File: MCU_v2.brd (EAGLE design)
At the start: 66 x 51.2 mm, 29 parts, among them IC1 ATMEGA2560-16AU

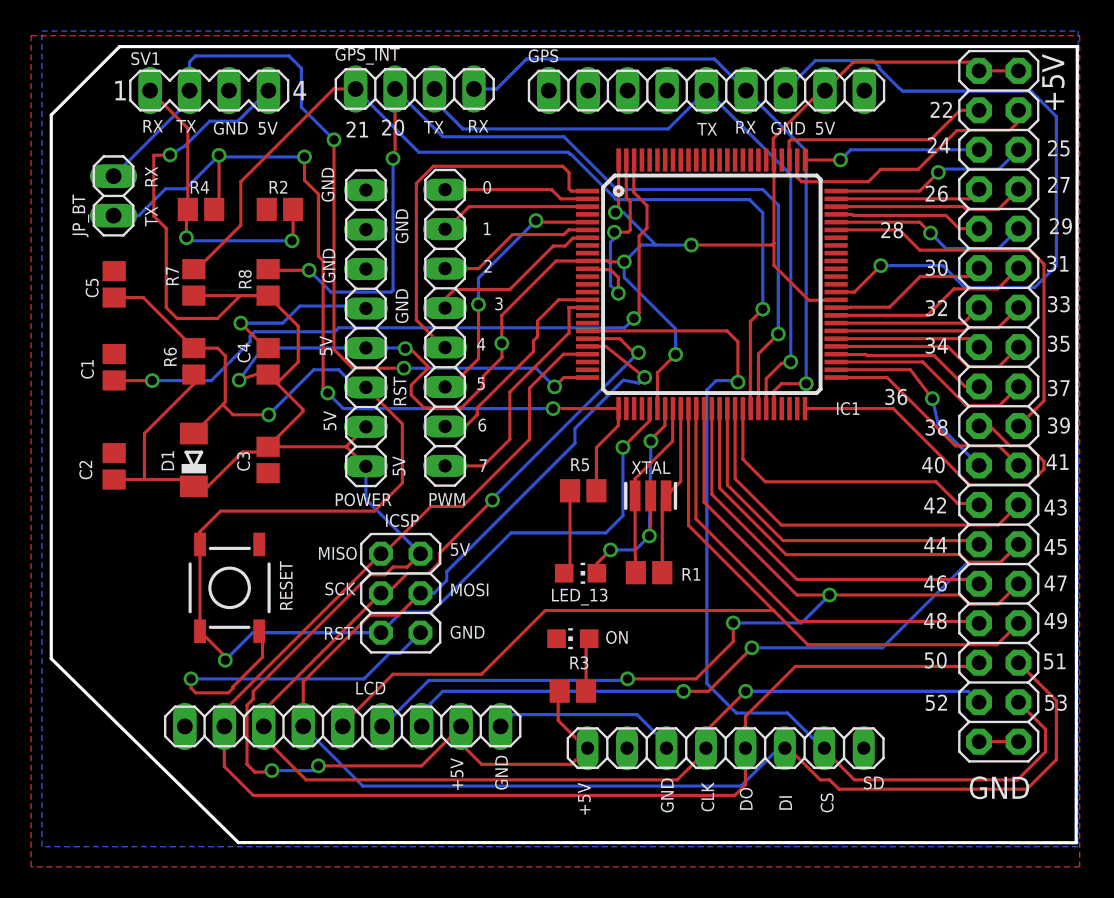
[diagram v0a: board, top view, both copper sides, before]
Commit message: Made the power traces thicker
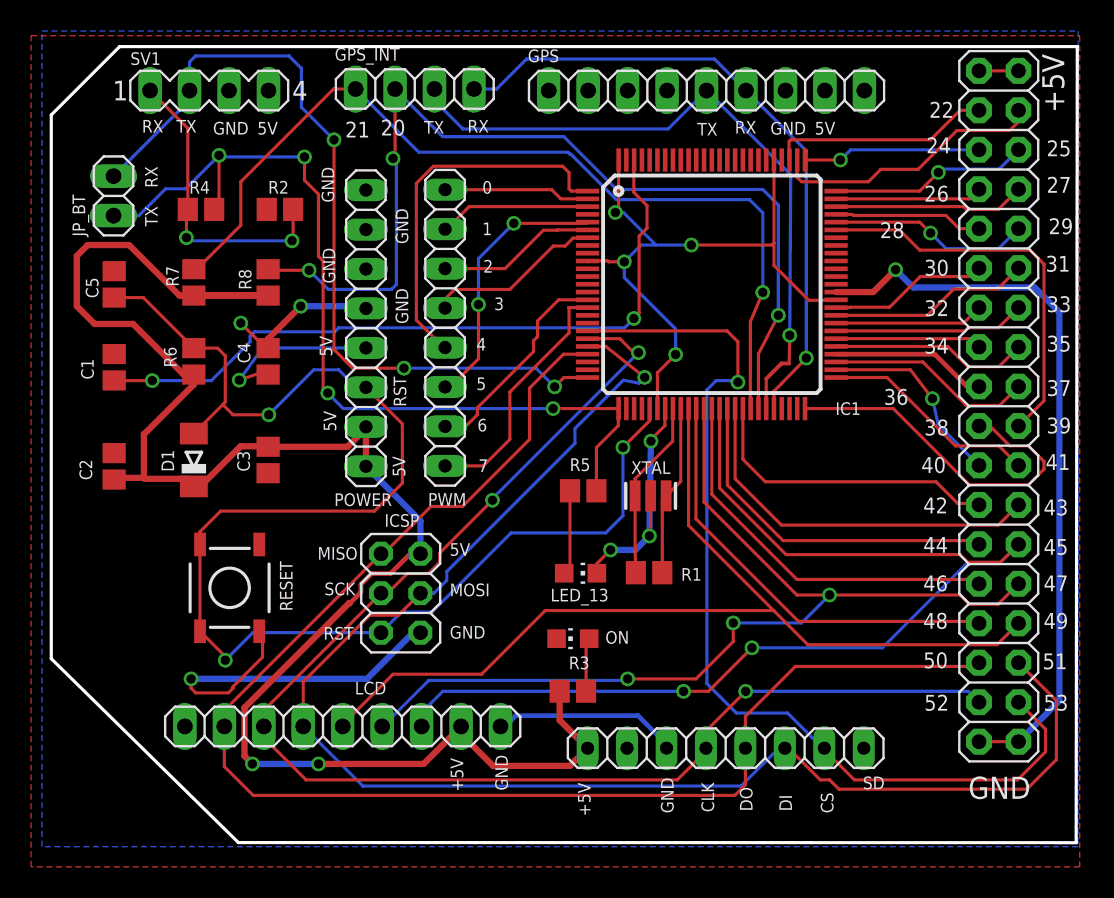
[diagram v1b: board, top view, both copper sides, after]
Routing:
- net +5V: track 226.8 -> 172.8 mm, vias 10 -> 7
- net GND: track 124.3 -> 109.7 mm, vias 8 -> 7
- net TXD1: track 43.0 -> 42.1 mm
- net PE3: track 16.7 -> 17.3 mm
